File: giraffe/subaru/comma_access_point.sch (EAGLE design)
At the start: 11 parts, among them J1 5018762640, J2 5018761040, J3 3-794618-2

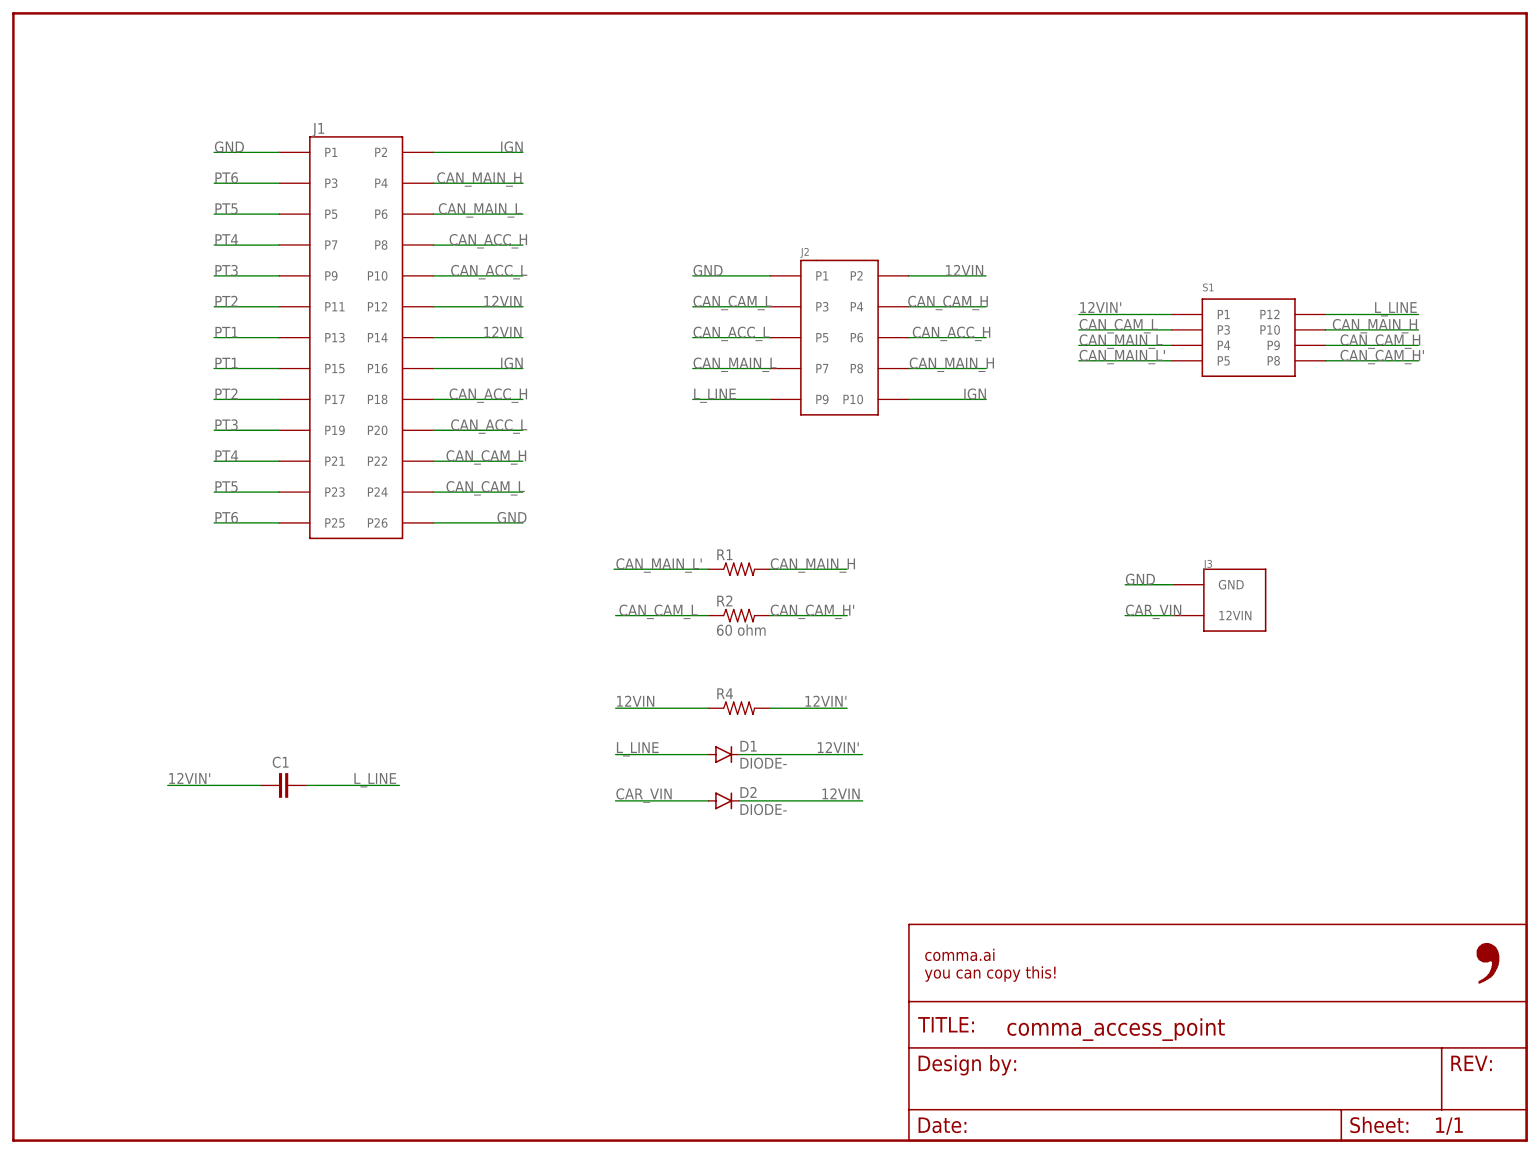
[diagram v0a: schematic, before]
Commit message: added UJA1023 to subaru giraffe on mlp's request
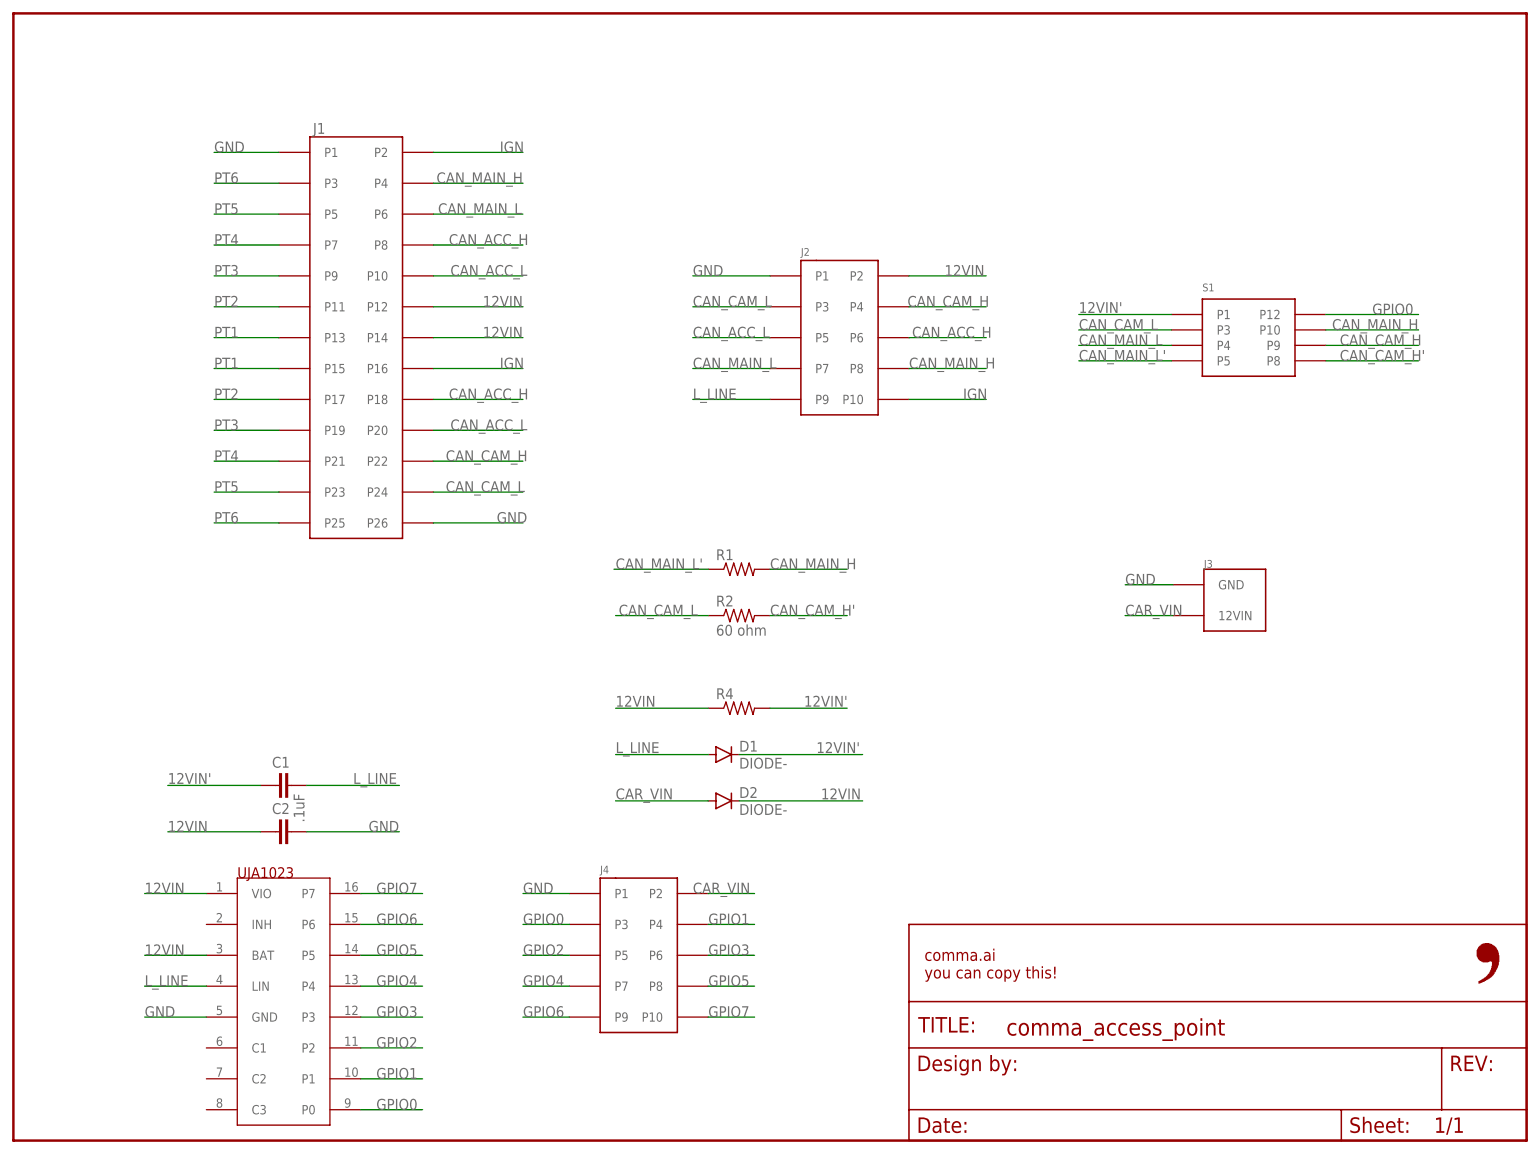
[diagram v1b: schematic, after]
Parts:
- added C2: .1uF, comma.ai:C0805
- added IC1: UJA1023, uja1023:UJA1023
- added J4: 5018761040, 5018761440:5018761040
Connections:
- new net GPIO0: IC1.P0, J4.P3, S1.P12
- new net GPIO1: IC1.P1, J4.P4
- new net GPIO2: IC1.P2, J4.P5
- new net GPIO3: IC1.P3, J4.P6
- new net GPIO4: IC1.P4, J4.P7
- new net GPIO5: IC1.P5, J4.P8
- new net GPIO6: IC1.P6, J4.P9
- new net GPIO7: IC1.P7, J4.P10
- net 12VIN: now also C2.1, IC1.BAT, IC1.VIO
- net CAR_VIN: now also J4.P2
- net GND: now also C2.2, IC1.GND, J4.P1
- net L_LINE: now also IC1.LIN; no longer S1.P12
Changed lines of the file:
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@@
 <?xml version="1.0" encoding="utf-8"?>
 <!DOCTYPE eagle SYSTEM "eagle.dtd">
-<eagle version="9.2.2">
+<eagle version="9.4.2">
 <drawing>
 <settings>
-<setting alwaysvectorfont="yes"/>
+<setting alwaysvectorfont="no"/>
 <setting verticaltext="up"/>
 </settings>
-<grid distance="0.1" unitdist="inch" unit="inch" style="lines" multiple="1" display="no" altdistance="0.01" altunitdist="inch" altunit="inch"/>
+<grid distance="0.1" unitdist="inch" unit="inch" style="lines" multiple="1" display="no" altdistance="0.05" altunitdist="inch" altunit="inch"/>
 <layers>
 <layer number="1" name="Top" color="4" fill="1" visible="no" active="no"/>
@@
 <part name="C1" library="comma.ai" library_urn="urn:adsk.eagle:library:2652900" deviceset="C" device="0805" package3d_urn="urn:adsk.eagle:package:2653203/1"/>
 <part name="D2" library="comma.ai" library_urn="urn:adsk.eagle:library:2652900" deviceset="DIODE" device="-" package3d_urn="urn:adsk.eagle:package:2653216/2"/>
+<part name="J4" library="5018761440" library_urn="urn:adsk.eagle:library:6968379" deviceset="5018761040" device="" package3d_urn="urn:adsk.eagle:package:6968387/2"/>
+<part name="IC1" library="uja1023" deviceset="UJA1023" device=""/>
+<part name="C2" library="comma.ai" library_urn="urn:adsk.eagle:library:2652900" deviceset="C" device="0805" package3d_urn="urn:adsk.eagle:package:2653203/1" value=".1uF"/>
 </parts>
 <sheets>
@@
 <attribute name="VALUE" x="119.38" y="53.5686" size="1.778" layer="96"/>
 </instance>
+<instance part="J4" gate="G$1" x="106.68" y="30.48" smashed="yes" rot="R270">
+<attribute name="NAME" x="96.52" y="43.942" size="1.27" layer="95"/>
+</instance>
+<instance part="IC1" gate="G$1" x="44.45" y="43.18" smashed="yes"/>
+<instance part="C2" gate="G$1" x="45.72" y="50.8" smashed="yes" rot="R90">
+<attribute name="NAME" x="45.466" y="55.499" size="1.778" layer="95" rot="R180"/>
+<attribute name="VALUE" x="47.879" y="52.324" size="1.778" layer="96" rot="R90"/>
+</instance>
 </instances>
 <busses>
@@
 <label x="132.842" y="56.134" size="1.778" layer="95"/>
 </segment>
+<segment>
+<wire x1="31.75" y1="40.64" x2="21.59" y2="40.64" width="0.1524" layer="91"/>
+<label x="21.59" y="40.64" size="1.778" layer="95"/>
+<pinref part="IC1" gate="G$1" pin="VIO"/>
+</segment>
+<segment>
+<pinref part="IC1" gate="G$1" pin="BAT"/>
+<wire x1="31.75" y1="30.48" x2="21.59" y2="30.48" width="0.1524" layer="91"/>
+<label x="21.59" y="30.48" size="1.778" layer="95"/>
+</segment>
+<segment>
+<pinref part="C2" gate="G$1" pin="1"/>
+<wire x1="40.64" y1="50.8" x2="25.4" y2="50.8" width="0.1524" layer="91"/>
+<label x="25.4" y="50.8" size="1.778" layer="95"/>
+</segment>
 </net>
 <net name="GND" class="0">
@@
 <label x="182.88" y="91.44" size="1.778" layer="95"/>
 </segment>
+<segment>
+<wire x1="31.75" y1="20.32" x2="21.59" y2="20.32" width="0.1524" layer="91"/>
+<label x="21.59" y="20.32" size="1.778" layer="95"/>
+<pinref part="IC1" gate="G$1" pin="GND"/>
+</segment>
+<segment>
+<pinref part="J4" gate="G$1" pin="P1"/>
+<wire x1="91.44" y1="40.64" x2="83.82" y2="40.64" width="0.1524" layer="91"/>
+<label x="83.82" y="40.64" size="1.778" layer="95"/>
+</segment>
+<segment>
+<pinref part="C2" gate="G$1" pin="2"/>
+<wire x1="48.26" y1="50.8" x2="63.5" y2="50.8" width="0.1524" layer="91"/>
+<label x="58.42" y="50.8" size="1.778" layer="95"/>
+</segment>
 </net>
 <net name="CAN_MAIN_L" class="0">
@@
 </segment>
 <segment>
-<pinref part="S1" gate="G$1" pin="P12"/>
-<wire x1="215.9" y1="135.89" x2="231.14" y2="135.89" width="0.1524" layer="91"/>
-<label x="223.774" y="136.144" size="1.778" layer="95"/>
+<wire x1="31.75" y1="25.4" x2="21.59" y2="25.4" width="0.1524" layer="91"/>
+<label x="21.59" y="25.4" size="1.778" layer="95"/>
+<pinref part="IC1" gate="G$1" pin="LIN"/>
 </segment>
 </net>
@@
 <label x="99.06" y="56.134" size="1.778" layer="95"/>
 </segment>
-</net>
+<segment>
+<pinref part="J4" gate="G$1" pin="P2"/>
+<wire x1="114.3" y1="40.64" x2="121.92" y2="40.64" width="0.1524" layer="91"/>
+<label x="111.76" y="40.64" size="1.778" layer="95"/>
+</segment>
+</net>
+<net name="GPIO7" class="0">
+<segment>
+<wire x1="57.15" y1="40.64" x2="67.31" y2="40.64" width="0.1524" layer="91"/>
+<label x="59.69" y="40.64" size="1.778" layer="95"/>
+<pinref part="IC1" gate="G$1" pin="P7"/>
+</segment>
+<segment>
+<pinref part="J4" gate="G$1" pin="P10"/>
+<wire x1="114.3" y1="20.32" x2="121.92" y2="20.32" width="0.1524" layer="91"/>
+<label x="114.3" y="20.32" size="1.778" layer="95"/>
+</segment>
+</net>
+<net name="GPIO6" class="0">
+<segment>
+<wire x1="57.15" y1="35.56" x2="67.31" y2="35.56" width="0.1524" layer="91"/>
+<label x="59.69" y="35.56" size="1.778" layer="95"/>
+<pinref part="IC1" gate="G$1" pin="P6"/>
+</segment>
+<segment>
+<pinref part="J4" gate="G$1" pin="P9"/>
+<wire x1="91.44" y1="20.32" x2="83.82" y2="20.32" width="0.1524" layer="91"/>
+<label x="83.82" y="20.32" size="1.778" layer="95"/>
+</segment>
+</net>
+<net name="GPIO5" class="0">
+<segment>
+<wire x1="57.15" y1="30.48" x2="67.31" y2="30.48" width="0.1524" layer="91"/>
+<label x="59.69" y="30.48" size="1.778" layer="95"/>
+<pinref part="IC1" gate="G$1" pin="P5"/>
+</segment>
+<segment>
+<pinref part="J4" gate="G$1" pin="P8"/>
+<wire x1="114.3" y1="25.4" x2="121.92" y2="25.4" width="0.1524" layer="91"/>
+<label x="114.3" y="25.4" size="1.778" layer="95"/>
+</segment>
+</net>
+<net name="GPIO4" class="0">
+<segment>
+<wire x1="57.15" y1="25.4" x2="67.31" y2="25.4" width="0.1524" layer="91"/>
+<label x="59.69" y="25.4" size="1.778" layer="95"/>
+<pinref part="IC1" gate="G$1" pin="P4"/>
+</segment>
+<segment>
+<pinref part="J4" gate="G$1" pin="P7"/>
+<wire x1="91.44" y1="25.4" x2="83.82" y2="25.4" width="0.1524" layer="91"/>
+<label x="83.82" y="25.4" size="1.778" layer="95"/>
+</segment>
+</net>
+<net name="GPIO3" class="0">
+<segment>
+<wire x1="57.15" y1="20.32" x2="67.31" y2="20.32" width="0.1524" layer="91"/>
+<label x="59.69" y="20.32" size="1.778" layer="95"/>
+<pinref part="IC1" gate="G$1" pin="P3"/>
+</segment>
+<segment>
+<pinref part="J4" gate="G$1" pin="P6"/>
+<wire x1="114.3" y1="30.48" x2="121.92" y2="30.48" width="0.1524" layer="91"/>
+<label x="114.3" y="30.48" size="1.778" layer="95"/>
+</segment>
+</net>
+<net name="GPIO2" class="0">
+<segment>
+<wire x1="57.15" y1="15.24" x2="67.31" y2="15.24" width="0.1524" layer="91"/>
+<label x="59.69" y="15.24" size="1.778" layer="95"/>
+<pinref part="IC1" gate="G$1" pin="P2"/>
+</segment>
+<segment>
+<pinref part="J4" gate="G$1" pin="P5"/>
+<wire x1="91.44" y1="30.48" x2="83.82" y2="30.48" width="0.1524" layer="91"/>
+<label x="83.82" y="30.48" size="1.778" layer="95"/>
+</segment>
+</net>
+<net name="GPIO1" class="0">
+<segment>
+<wire x1="57.15" y1="10.16" x2="67.31" y2="10.16" width="0.1524" layer="91"/>
+<label x="59.69" y="10.16" size="1.778" layer="95"/>
+<pinref part="IC1" gate="G$1" pin="P1"/>
+</segment>
+<segment>
+<pinref part="J4" gate="G$1" pin="P4"/>
+<wire x1="114.3" y1="35.56" x2="121.92" y2="35.56" width="0.1524" layer="91"/>
+<label x="114.3" y="35.56" size="1.778" layer="95"/>
+</segment>
+</net>
+<net name="GPIO0" class="0">
+<segment>
+<wire x1="57.15" y1="5.08" x2="67.31" y2="5.08" width="0.1524" layer="91"/>
+<label x="59.69" y="5.08" size="1.778" layer="95"/>
+<pinref part="IC1" gate="G$1" pin="P0"/>
+</segment>
+<segment>
+<pinref part="S1" gate="G$1" pin="P12"/>
+<wire x1="215.9" y1="135.89" x2="231.14" y2="135.89" width="0.1524" layer="91"/>
+<label x="223.52" y="135.89" size="1.778" layer="95"/>
+</segment>
+<segment>
+<pinref part="J4" gate="G$1" pin="P3"/>
+<wire x1="91.44" y1="35.56" x2="83.82" y2="35.56" width="0.1524" layer="91"/>
+<label x="83.82" y="35.56" size="1.778" layer="95"/>
+</segment>
+</net>
